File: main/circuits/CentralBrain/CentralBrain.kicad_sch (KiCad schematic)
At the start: 49 parts, among them J1 WAGO 12V IN, J2 WAGO 12V IN, J3 WAGE 12V IN, U1 MAX485E, U10 AM26C31CN, U11 AM26C31CN, U2 SN74HCT245N, U3 Teensy4.1_Minimal, U4 SN74HCT245N, U5 SN74HCT245N, U6 AM26C31CN, U7 AM26C31CN, U8 AM26C31CN, U9 AM26C31CN

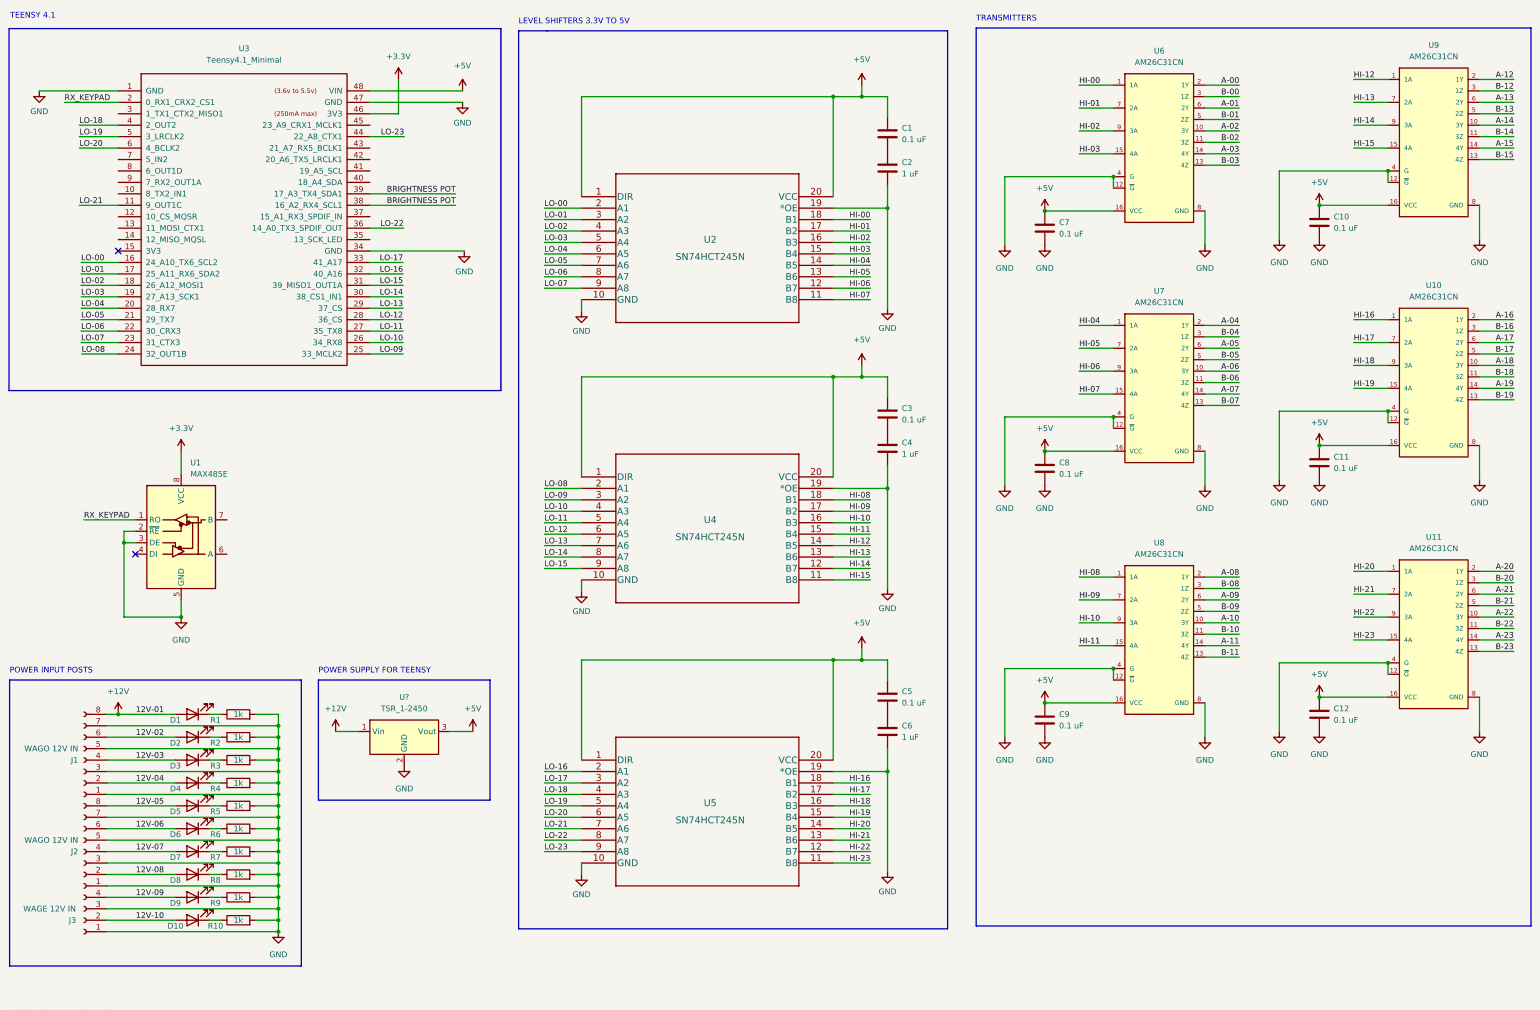
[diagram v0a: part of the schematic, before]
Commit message: no need for level shifters! thanks chuck!
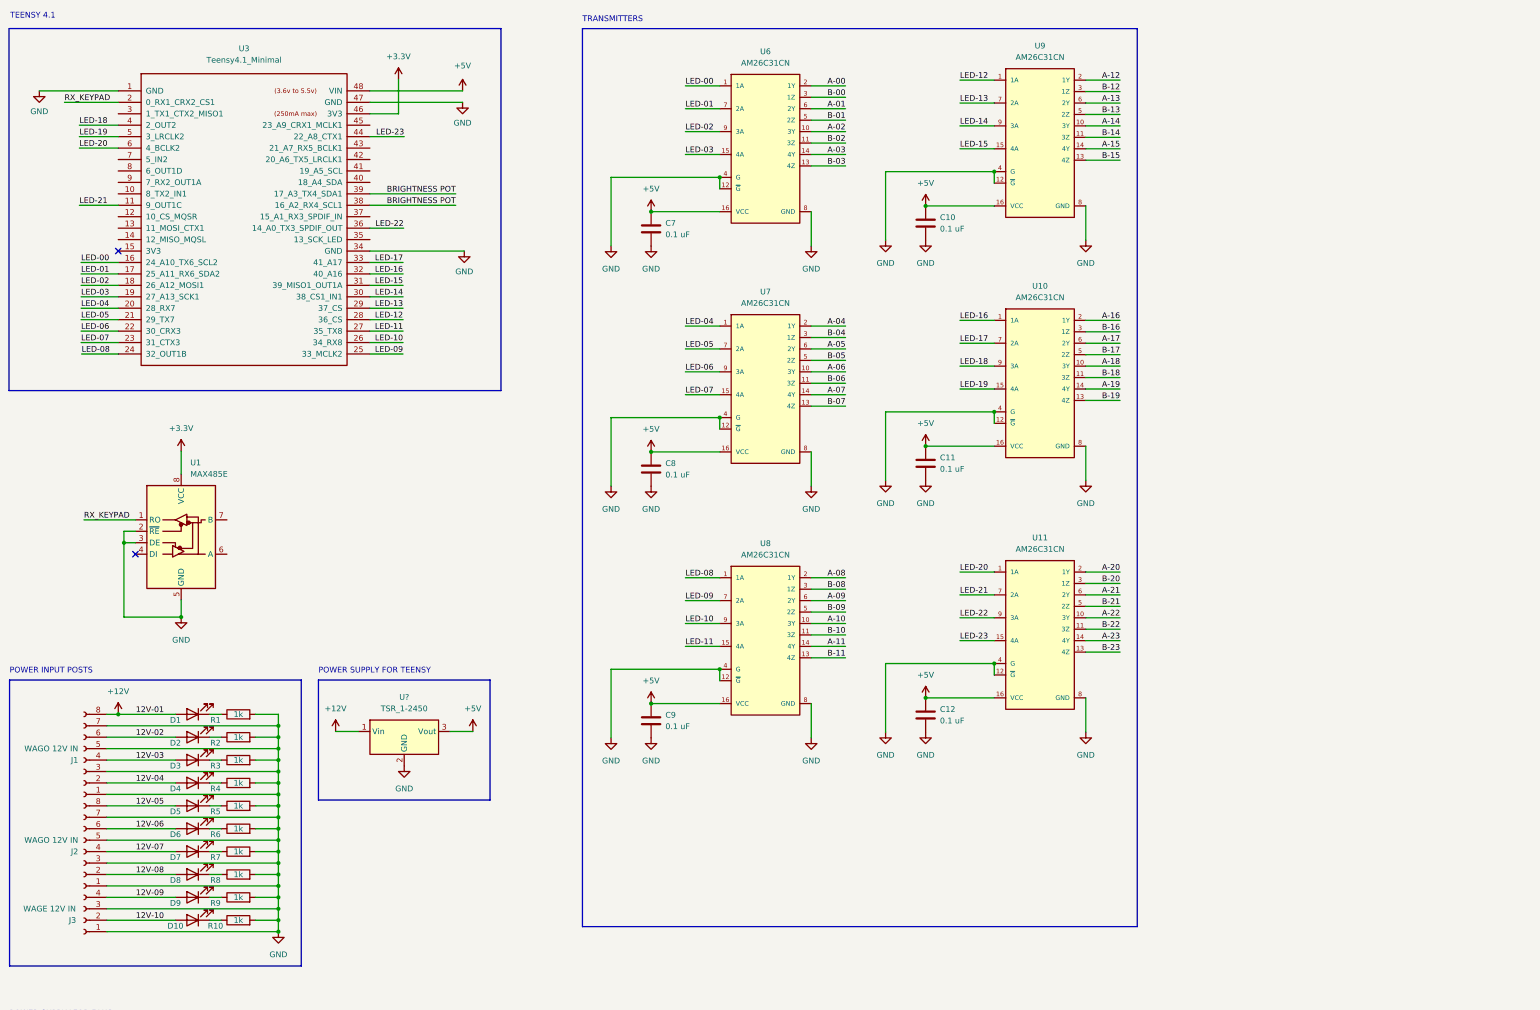
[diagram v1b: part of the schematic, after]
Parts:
- removed C1, C3, C5: 0.1 uF, symbol Device:C
- removed C2, C4, C6: 1 uF, symbol Device:C
- removed U2, U4, U5: SN74HCT245N, N20, symbol Joels KiCad Symbol Library:SN74HCT245N
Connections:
- net LO-00 is gone; now on net LED-00: U3.16 (24_A10_TX6_SCL2)
- net LO-01 is gone; now on net LED-01: U3.17 (25_A11_RX6_SDA2)
- net LO-02 is gone; now on net LED-02: U3.18 (26_A12_MOSI1)
- net LO-03 is gone; now on net LED-03: U3.19 (27_A13_SCK1)
- net LO-04 is gone; now on net LED-04: U3.20 (28_RX7)
- net LO-05 is gone; now on net LED-05: U3.21 (29_TX7)
- net LO-06 is gone; now on net LED-06: U3.22 (30_CRX3)
- net LO-07 is gone; now on net LED-07: U3.23 (31_CTX3)
- net LO-08 is gone; now on net LED-08: U3.24 (32_OUT1B)
- net LO-09 is gone; now on net LED-09: U3.25 (33_MCLK2)
- net LO-10 is gone; now on net LED-10: U3.26 (34_RX8)
- net LO-11 is gone; now on net LED-11: U3.27 (35_TX8)
- net LO-12 is gone; now on net LED-12: U3.28 (36_CS)
- net LO-13 is gone; now on net LED-13: U3.29 (37_CS)
- net LO-14 is gone; now on net LED-14: U3.30 (38_CS1_IN1)
- net LO-15 is gone; now on net LED-15: U3.31 (39_MISO1_OUT1A)
- net LO-16 is gone; now on net LED-16: U3.32 (40_A16)
- net LO-17 is gone; now on net LED-17: U3.33 (41_A17)
- net LO-18 is gone; now on net LED-18: U3.4 (2_OUT2)
- net LO-19 is gone; now on net LED-19: U3.5 (3_LRCLK2)
- net LO-20 is gone; now on net LED-20: U3.6 (4_BCLK2)
- net LO-21 is gone; now on net LED-21: U3.11 (9_OUT1C)
- net LO-22 is gone; now on net LED-22: U3.36 (14_A0_TX3_SPDIF_OUT)
- net LO-23 is gone; now on net LED-23: U3.44 (22_A8_CTX1)
- net HI-00 renamed LED-00
- net HI-01 renamed LED-01
- net HI-02 renamed LED-02
- net HI-03 renamed LED-03
- net HI-04 renamed LED-04
- net HI-05 renamed LED-05
- net HI-06 renamed LED-06
- net HI-07 renamed LED-07
- net HI-08 renamed LED-08
- net HI-09 renamed LED-09
- net HI-10 renamed LED-10
- net HI-11 renamed LED-11
- net HI-12 renamed LED-12
- net HI-13 renamed LED-13
- net HI-14 renamed LED-14
- net HI-15 renamed LED-15
- net HI-16 renamed LED-16
- net HI-17 renamed LED-17
- net HI-18 renamed LED-18
- net HI-19 renamed LED-19
- net HI-20 renamed LED-20
- net HI-21 renamed LED-21
- net HI-22 renamed LED-22
- net HI-23 renamed LED-23
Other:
- note removed: "LEVEL SHIFTERS 3.3V TO 5V"
- moved on the sheet: C10, C11, C12, C7, C8, C9, U10, U11, U6, U7, U8, U9

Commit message: started work on the central PCB
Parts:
- removed J1, J2: WAGO 12V IN, symbol Connector:Conn_01x08_Female
- removed J3: WAGE 12V IN, symbol Connector:Conn_01x04_Female
- removed J?: FAN, symbol Connector:Conn_01x02_Female
- removed U?: TSR_1-2450, Converter_DCDC:Converter_DCDC_TRACO_TSR-1_THT, symbol Regulator_Switching:TSR_1-2450
- added J1: POWER 1234, Joels KiCad Footprint Library:WAGO-2604-1308, symbol Joels KiCad Symbol Library:WAGO-2604-1308
- added J2: POWER 5678, Joels KiCad Footprint Library:WAGO-2604-1308, symbol Joels KiCad Symbol Library:WAGO-2604-1308
- added J3: POWER 910, Joels KiCad Footprint Library:WAGO-2604-1304, symbol Joels KiCad Symbol Library:WAGO-2604-1304
- added J4: EXTRA_TEENSY_PINS, Joels KiCad Footprint Library:CUI_term_block_8_TB004-508-08BE, symbol Connector:Conn_01x08_Female
- added J5: RJ45, Joels KiCad Footprint Library:TE_5569264-1_16_Port_RJ45, symbol Joels KiCad Symbol Library:TE_5569264-1_16_PORT_RJ45
- added J6: TE_5569262-1_08_PORT_RJ45, Joels KiCad Footprint Library:TE_5569262-1_08_Port_RJ45_New, symbol Joels KiCad Symbol Library:TE_5569262-1_08_PORT_RJ45
- added J7: RJ45_Shielded, Joels KiCad Footprint Library:RJ45-ASSMANN_A-2004-1-4-LP-N-R, symbol Connector:RJ45_Shielded
- added J8: AUDIO_PINS, Joels KiCad Footprint Library:CUI_term_block_8_TB004-508-08BE, symbol Connector:Conn_01x08_Female
- added RV1, RV2: 100K, Potentiometer_THT:Potentiometer_Alpha_RD901F-40-00D_Single_Vertical, symbol Device:R_Potentiometer_US
- added U5: Teensy4.0_AudioShield_REVD, Joels KiCad Footprint Library:Teensy4.0_Audioshield_RevD, symbol Joels KiCad Symbol Library:Teensy4.0_AudioShield_REVD
- C1: renamed from C7; footprint (none) -> Capacitor_SMD:C_0805_2012Metric_Pad1.18x1.45mm_HandSolder
- C2: renamed from C10; footprint (none) -> Capacitor_SMD:C_0805_2012Metric_Pad1.18x1.45mm_HandSolder
- C3: renamed from C8; footprint (none) -> Capacitor_SMD:C_0805_2012Metric_Pad1.18x1.45mm_HandSolder
- C4: renamed from C11; footprint (none) -> Capacitor_SMD:C_0805_2012Metric_Pad1.18x1.45mm_HandSolder
- C5: renamed from C9; footprint (none) -> Capacitor_SMD:C_0805_2012Metric_Pad1.18x1.45mm_HandSolder
- C6: renamed from C12; footprint (none) -> Capacitor_SMD:C_0805_2012Metric_Pad1.18x1.45mm_HandSolder
- D1, D10, D2, D3, D4, D5, D6, D7, D8, D9: footprint (none) -> LED_THT:LED_D3.0mm
- R1, R10, R2, R3, R4, R5, R6, R7, R8, R9: value 1k -> 4.7k; footprint (none) -> Resistor_THT:R_Axial_DIN0207_L6.3mm_D2.5mm_P7.62mm_Horizontal
- U1: footprint (none) -> Joels KiCad Footprint Library:Max485-Module
- U10, U11, U6, U7, U8, U9: footprint Texas_Instruments-AM26C31CDR-* -> Joels KiCad Footprint Library:AM26C31CN
- U3: footprint (none) -> Joels KiCad Footprint Library:Teensy41_Minimal
- gave numbers to parts that had none: 1
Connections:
- net +12V: now also J1.1, J1.2, J5.1, J5.10 (2), J5.11 (3), J5.2, J5.3, J5.9 (1), J7.1, J7.2, J7.3
- net +3V3: now also J8.1 (Pin_1), RV1.3, RV2.3, U5.28 (3V)
- net +5V: now also J4.1 (Pin_1)
- net 12V-02: now also J1.5, J1.6, J5.17 (1), J5.18 (2), J5.19 (3), J5.25 (1), J5.26 (2), J5.27 (3)
- net 12V-03: now also J1.10, J1.9, J5.33 (1), J5.34 (2), J5.35 (3), J5.41 (1), J5.42 (2), J5.43 (3)
- net 12V-04: now also J1.13, J1.14, J5.49 (1), J5.50 (2), J5.51 (3), J5.57 (1), J5.58 (2), J5.59 (3)
- net 12V-05: now also J2.1, J2.2, J5.65 (1), J5.66 (2), J5.67 (3), J5.73 (1), J5.74 (2), J5.75 (3)
- net 12V-06: now also J2.5, J2.6, J5.81 (1), J5.82 (2), J5.83 (3), J5.89 (1), J5.90 (2), J5.91 (3)
- net 12V-07: now also J2.10, J2.9, J5.105 (1), J5.106 (2), J5.107 (3), J5.113 (1), J5.114 (2), J5.115 (3), J5.97 (1), J5.98 (2), J5.99 (3)
- net 12V-08: now also J2.13, J2.14, J5.121 (1), J5.122 (2), J5.123 (3), J6.14, J6.15, J6.16, J6.6, J6.7, J6.8
- net 12V-09: now also J3.1, J3.2, J6.22, J6.23, J6.24, J6.30, J6.31, J6.32, J6.33, J6.34, J6.35
- net 12V-10: now also J3.5, J3.6, J6.41, J6.42, J6.43, J6.49, J6.50, J6.51, J6.57, J6.58, J6.59
- net A-00: now also J5.4
- net A-01: now also J5.12 (4)
- net A-02: now also J5.20 (4)
- net A-03: now also J5.28 (4)
- net A-04: now also J5.36 (4)
- net A-05: now also J5.44 (4)
- net A-06: now also J5.52 (4)
- net A-07: now also J5.60 (4)
- net A-08: now also J5.68 (4)
- net A-09: now also J5.76 (4)
- net A-10: now also J5.84 (4)
- net A-11: now also J5.92 (4)
- net A-12: now also J5.100 (4)
- net A-13: now also J5.108 (4)
- net A-14: now also J5.116 (4)
- net A-15: now also J5.124 (4)
- net A-16: now also J6.5
- net A-17: now also J6.36
- net A-18: now also J6.44
- net A-19: now also J6.13
- net A-20: now also J6.21
- net A-21: now also J6.52
- net A-22: now also J6.60
- net A-23: now also J6.29
- net B-00: now also J5.5
- net B-01: now also J5.13 (5)
- net B-02: now also J5.21 (5)
- net B-03: now also J5.29 (5)
- net B-04: now also J5.37 (5)
- net B-05: now also J5.45 (5)
- net B-06: now also J5.53 (5)
- net B-07: now also J5.61 (5)
- net B-08: now also J5.69 (5)
- net B-09: now also J5.77 (5)
- net B-10: now also J5.85 (5)
- net B-11: now also J5.93 (5)
- net B-12: now also J5.101 (5)
- net B-13: now also J5.109 (5)
- net B-14: now also J5.117 (5)
- net B-15: now also J5.125 (5)
- net B-16: now also J6.4
- net B-17: now also J6.37
- net B-18: now also J6.45
- net B-19: now also J6.12
- net B-20: now also J6.20
- net B-21: now also J6.53
- net B-22: now also J6.61
- net B-23: now also J6.28
- net GND: now also J1.11, J1.12, J1.15, J1.16, J1.3, J1.4, J1.7, J1.8, J2.11, J2.12, J2.15, J2.16, J2.3, J2.4, J2.7, J2.8, J3.3, J3.4, J3.7, J3.8, J4.8 (Pin_8), J5.102 (6), J5.103 (7), J5.104 (8), J5.110 (6), J5.111 (7), J5.112 (8), J5.118 (6), J5.119 (7), J5.120 (8), J5.126 (6), J5.127 (7), J5.128 (8), J5.14 (6), J5.15 (7), J5.16 (8), J5.22 (6), J5.23 (7), J5.24 (8), J5.30 (6), J5.31 (7), J5.32 (8), J5.38 (6), J5.39 (7), J5.40 (8), J5.46 (6), J5.47 (7), J5.48 (8), J5.54 (6), J5.55 (7), J5.56 (8), J5.6, J5.62 (6), J5.63 (7), J5.64 (8), J5.7, J5.70 (6), J5.71 (7), J5.72 (8), J5.78 (6), J5.79 (7), J5.8, J5.80 (8), J5.86 (6), J5.87 (7), J5.88 (8), J5.94 (6), J5.95 (7), J5.96 (8), J5.SH1 (SHIELD), J5.SH2 (SHIELD), J5.SH3 (SHIELD), J5.SH4 (SHIELD), J5.SH5 (SHIELD), J5.SH6 (SHIELD), J6.1, J6.10, J6.11, J6.17, J6.18, J6.19, J6.2, J6.25, J6.26, J6.27, J6.3, J6.38, J6.39, J6.40, J6.46, J6.47, J6.48, J6.54, J6.55, J6.56, J6.62, J6.63, J6.64, J6.67 (SH67), J6.68 (SH68), J6.69 (SH69), J6.70 (SH70), J6.71 (SH71), J6.72 (SH72), J6.9, J7.6, J7.7, J7.8, J7.S1, J7.S2, J8.6 (Pin_6), J8.7 (Pin_7), J8.8 (Pin_8), RV1.1, RV2.1, U5.1 (GND), U5.29 (GND)
- net at U1.6 (A): now also J7.5
- net at U1.7 (B): now also J7.4
- net AUDIO_DOUT: now reaches U3.10 (8_TX2_IN1)
- net AUDIO_DOUT: now also U5.10 (8_TX2_IN1)
- net PIN_10: now reaches U3.12 (10_CS_MQSR)
- net PIN_10: now also J4.2 (Pin_2)
- net PIN_11: now reaches U3.13 (11_MOSI_CTX1)
- net PIN_11: now also J4.3 (Pin_3)
- net PIN_12: now reaches U3.14 (12_MISO_MQSL)
- net PIN_12: now also J4.4 (Pin_4)
- net PIN_1: now reaches U3.3 (1_TX1_CTX2_MISO1)
- net PIN_1: now also J4.6 (Pin_6)
- net PIN_15: now reaches U3.37 (15_A1_RX3_SPDIF_IN)
- net PIN_15: now also J4.5 (Pin_5)
- net AUDIO_SDA: now reaches U3.40 (18_A4_SDA)
- net AUDIO_SDA: now also U5.22 (18_A4_SDA0)
- net AUDIO_SCL: now reaches U3.41 (19_A5_SCL)
- net AUDIO_SCL: now also U5.23 (19_A5_SCL0)
- net AUDIO_LRCLK: now reaches U3.42 (20_A6_TX5_LRCLK1)
- net AUDIO_LRCLK: now also U5.24 (20_A6_TX5_LRCLK1)
- net AUDIO_BCLK: now reaches U3.43 (21_A7_RX5_BCLK1)
- net AUDIO_BCLK: now also U5.25 (21_A7_RX5_BCLK1)
- net AUDIO_MCLK: now reaches U3.45 (23_A9_CRX1_MCLK1)
- net AUDIO_MCLK: now also U5.27 (23_A9_CRX1_MCLK1)
- net PHONE_JACK_SW: now reaches U3.7 (5_IN2)
- net PHONE_JACK_SW: now also J8.5 (Pin_5)
- net PIN_6: now reaches U3.8 (6_OUT1D)
- net PIN_6: now also J4.7 (Pin_7)
- net AUDIO_DIN: now reaches U3.9 (7_RX2_OUT1A)
- net AUDIO_DIN: now also U5.9 (7_RX2_OUT1A)
- net BRIGHTNESS POT renamed POT_ANTENNA
- net POT_ANTENNA: now also RV1.2; no longer U3.38 (16_A2_RX4_SCL1)
- new net AUDIO_LINE_IN_GND: J8.2 (Pin_2), U5.36 (LINE_IN_R_GND), U5.37 (LINE_IN_L_GND)
- new net AUDIO_LINE_IN_L: J8.3 (Pin_3), U5.35 (LINE_IN_L)
- new net AUDIO_LINE_IN_R: J8.4 (Pin_4), U5.34 (LINE_IN_R)
- new net POT_WHIPS: RV2.2, U3.38 (16_A2_RX4_SCL1)
- no-connect marks 2 -> 34
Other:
- note added: "A LOT OF RJ-45 OUTPUT"
- note added: "AUDIO PINS AND EXTRA PINS"
- note added: "AUDIO SHIELD"
- note added: "BRIGHTNESS POTENTIOMETERS"
- note added: "CONNECTION TO KEYBOARD"
- note added: "DC POWER SUPPLY CONNECTION"
- note added: "FOR ANTENNA"
- note added: "FOR WHIPS"
- note added: "POWER INDICATOR LAMPS"
- note added: "T568B COLOR CODE 1 ORA . . . 12V 2 ORA --- 12V 3 GRN . . . 12V 4 BLU --- A 5 BLU . . . B 6 GRN --- GND 7 BRN . . . GND 8 BRN --- GND"
- note removed: "POWER INPUT POSTS"
- note removed: "POWER SUPPLY FOR FANS"
- moved on the sheet: C1, C2, C3, C4, C5, C6, D1, D10, D2, D3, D4, D5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

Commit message: lots of work on pcb
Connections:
- net A-00: now also J5.20 (4); no longer J5.4
- net A-01: now also J5.84 (4); no longer J5.12 (4)
- net A-02: now also J5.92 (4); no longer J5.20 (4)
- net A-05: now also J5.100 (4); no longer J5.44 (4)
- net A-06: now also J5.108 (4); no longer J5.52 (4)
- net A-07: now also J5.44 (4); no longer J5.60 (4)
- net A-08: now also J5.4; no longer J5.68 (4)
- net A-09: now also J5.68 (4); no longer J5.76 (4)
- net A-10: now also J5.76 (4); no longer J5.84 (4)
- net A-11: now also J5.12 (4); no longer J5.92 (4)
- net A-12: now also J5.52 (4); no longer J5.100 (4)
- net A-13: now also J5.116 (4); no longer J5.108 (4)
- net A-14: now also J5.124 (4); no longer J5.116 (4)
- net A-15: now also J5.60 (4); no longer J5.124 (4)
- net B-00: now also J5.21 (5); no longer J5.5
- net B-01: now also J5.85 (5); no longer J5.13 (5)
- net B-02: now also J5.93 (5); no longer J5.21 (5)
- net B-05: now also J5.101 (5); no longer J5.45 (5)
- net B-06: now also J5.109 (5); no longer J5.53 (5)
- net B-07: now also J5.45 (5); no longer J5.61 (5)
- net B-08: now also J5.5; no longer J5.69 (5)
- net B-09: now also J5.69 (5); no longer J5.77 (5)
- net B-10: now also J5.77 (5); no longer J5.85 (5)
- net B-11: now also J5.13 (5); no longer J5.93 (5)
- net B-12: now also J5.53 (5); no longer J5.101 (5)
- net B-13: now also J5.117 (5); no longer J5.109 (5)
- net B-14: now also J5.125 (5); no longer J5.117 (5)
- net B-15: now also J5.61 (5); no longer J5.125 (5)
- net LED-00: now also U3.30 (38_CS1_IN1); no longer U3.16 (24_A10_TX6_SCL2)
- net LED-01: now also U3.31 (39_MISO1_OUT1A); no longer U3.17 (25_A11_RX6_SDA2)
- net LED-02: now also U3.28 (36_CS); no longer U3.18 (26_A12_MOSI1)
- net LED-03: now also U3.29 (37_CS); no longer U3.19 (27_A13_SCK1)
- net LED-04: now also U3.26 (34_RX8); no longer U3.20 (28_RX7)
- net LED-05: now also U3.27 (35_TX8); no longer U3.21 (29_TX7)
- net LED-06: now also U3.24 (32_OUT1B); no longer U3.22 (30_CRX3)
- net LED-07: now also U3.25 (33_MCLK2); no longer U3.23 (31_CTX3)
- net LED-08: now also U3.36 (14_A0_TX3_SPDIF_OUT); no longer U3.24 (32_OUT1B)
- net LED-09: now also U3.44 (22_A8_CTX1); no longer U3.25 (33_MCLK2)
- net LED-10: now also U3.32 (40_A16); no longer U3.26 (34_RX8)
- net LED-11: now also U3.33 (41_A17); no longer U3.27 (35_TX8)
- net LED-12: now also U3.22 (30_CRX3); no longer U3.28 (36_CS)
- net LED-13: now also U3.23 (31_CTX3); no longer U3.29 (37_CS)
- net LED-14: now also U3.20 (28_RX7); no longer U3.30 (38_CS1_IN1)
- net LED-15: now also U3.21 (29_TX7); no longer U3.31 (39_MISO1_OUT1A)
- net LED-16: now also U3.18 (26_A12_MOSI1); no longer U3.32 (40_A16)
- net LED-17: now also U3.19 (27_A13_SCK1); no longer U3.33 (41_A17)
- net LED-18: now also U3.16 (24_A10_TX6_SCL2); no longer U3.4 (2_OUT2)
- net LED-19: now also U3.17 (25_A11_RX6_SDA2); no longer U3.5 (3_LRCLK2)
- net LED-22: now also U3.4 (2_OUT2); no longer U3.36 (14_A0_TX3_SPDIF_OUT)
- net LED-23: now also U3.5 (3_LRCLK2); no longer U3.44 (22_A8_CTX1)

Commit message: Mechanical design of PCB mostly done
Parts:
- added H1, H3, H4, H6: MountingHole, MountingHole:MountingHole_3.5mm, symbol Mechanical:MountingHole
- J6: footprint Joels KiCad Footprint Library:TE_5569262-1_08_Port_RJ45_New -> Joels KiCad Footprint Library:TE_5569262-1_08_Port_RJ45
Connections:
- net +12V: now also J5.121 (1), J5.122 (2), J5.123 (3), J5.49 (1), J5.50 (2), J5.51 (3), J5.57 (1), J5.58 (2), J5.59 (3); no longer J5.1, J5.10 (2), J5.11 (3), J5.2, J5.3, J5.9 (1)
- net LED-00: now also U3.24 (32_OUT1B); no longer U3.30 (38_CS1_IN1)
- net LED-01: now also U3.25 (33_MCLK2); no longer U3.31 (39_MISO1_OUT1A)
- net LED-02: now also U3.26 (34_RX8); no longer U3.28 (36_CS)
- net LED-03: now also U3.27 (35_TX8); no longer U3.29 (37_CS)
- net LED-04: now also U3.28 (36_CS); no longer U3.26 (34_RX8)
- net LED-05: now also U3.29 (37_CS); no longer U3.27 (35_TX8)
- net LED-06: now also U3.30 (38_CS1_IN1); no longer U3.24 (32_OUT1B)
- net LED-07: now also U3.31 (39_MISO1_OUT1A); no longer U3.25 (33_MCLK2)
- net LED-08: now also U3.20 (28_RX7); no longer U3.36 (14_A0_TX3_SPDIF_OUT)
- net LED-09: now also U3.21 (29_TX7); no longer U3.44 (22_A8_CTX1)
- net LED-10: now also U3.22 (30_CRX3); no longer U3.32 (40_A16)
- net LED-11: now also U3.23 (31_CTX3); no longer U3.33 (41_A17)
- net LED-12: now also U3.32 (40_A16); no longer U3.22 (30_CRX3)
- net LED-13: now also U3.33 (41_A17); no longer U3.23 (31_CTX3)
- net LED-14: now also U3.36 (14_A0_TX3_SPDIF_OUT); no longer U3.20 (28_RX7)
- net LED-15: now also U3.44 (22_A8_CTX1); no longer U3.21 (29_TX7)
- net LED-16: now also U3.4 (2_OUT2); no longer U3.18 (26_A12_MOSI1)
- net LED-17: now also U3.5 (3_LRCLK2); no longer U3.19 (27_A13_SCK1)
- net LED-18: now also U3.6 (4_BCLK2); no longer U3.16 (24_A10_TX6_SCL2)
- net LED-19: now also U3.11 (9_OUT1C); no longer U3.17 (25_A11_RX6_SDA2)
- net LED-20: now also U3.16 (24_A10_TX6_SCL2); no longer U3.6 (4_BCLK2)
- net LED-21: now also U3.17 (25_A11_RX6_SDA2); no longer U3.11 (9_OUT1C)
- net LED-22: now also U3.18 (26_A12_MOSI1); no longer U3.4 (2_OUT2)
- net LED-23: now also U3.19 (27_A13_SCK1); no longer U3.5 (3_LRCLK2)
- net PIN_1: now also J4.2 (Pin_2); no longer J4.6 (Pin_6)
- net PIN_10: now also J4.4 (Pin_4); no longer J4.2 (Pin_2)
- net PIN_11: now also J4.5 (Pin_5); no longer J4.3 (Pin_3)
- net PIN_12: now also J4.6 (Pin_6); no longer J4.4 (Pin_4)
- net PIN_15: now also J4.7 (Pin_7); no longer J4.5 (Pin_5)
- net PIN_6: now also J4.3 (Pin_3); no longer J4.7 (Pin_7)
- removed net 12V-02: D2.2 (A), J1.5, J1.6, J5.17 (1), J5.18 (2), J5.19 (3), J5.25 (1), J5.26 (2), J5.27 (3)
- net 12V-03 renamed 12V_03
- net 12V_03: now also J5.25 (1), J5.26 (2), J5.27 (3), J5.97 (1), J5.98 (2), J5.99 (3); no longer J5.41 (1), J5.42 (2), J5.43 (3)
- removed net 12V-04: D4.2 (A), J1.13, J1.14, J5.49 (1), J5.50 (2), J5.51 (3), J5.57 (1), J5.58 (2), J5.59 (3)
- net 12V-05 renamed 12V_05
- net 12V_05: now also J5.10 (2), J5.11 (3), J5.9 (1); no longer J5.65 (1), J5.66 (2), J5.67 (3)
- net 12V-06 renamed 12V_04
- net 12V_04: now also D4.2 (A), J1.13, J1.14, J5.17 (1), J5.18 (2), J5.19 (3); no longer D6.2 (A), J2.5, J2.6
- net 12V-07 renamed 12V_02
- net 12V_02: now also D2.2 (A), J1.5, J1.6, J5.41 (1), J5.42 (2), J5.43 (3); no longer D7.2 (A), J2.10, J2.9, J5.97 (1), J5.98 (2), J5.99 (3)
- removed net 12V-08: D8.2 (A), J2.13, J2.14, J5.121 (1), J5.122 (2), J5.123 (3), J6.14, J6.15, J6.16, J6.6, J6.7, J6.8
- removed net 12V-09: D9.2 (A), J3.1, J3.2, J6.22, J6.23, J6.24, J6.30, J6.31, J6.32, J6.33, J6.34, J6.35
- removed net 12V-10: D10.2 (A), J3.5, J3.6, J6.41, J6.42, J6.43, J6.49, J6.50, J6.51, J6.57, J6.58, J6.59
- new net 12V_06: D6.2 (A), J2.5, J2.6, J5.1, J5.2, J5.3, J5.65 (1), J5.66 (2), J5.67 (3)
- new net 12V_07: D7.2 (A), J2.10, J2.9, J6.30, J6.31, J6.32, J6.57, J6.58, J6.59
- new net 12V_08: D8.2 (A), J2.13, J2.14, J6.22, J6.23, J6.24, J6.49, J6.50, J6.51
- new net 12V_09: D9.2 (A), J3.1, J3.2, J6.14, J6.15, J6.16, J6.41, J6.42, J6.43
- new net 12V_10: D10.2 (A), J3.5, J3.6, J6.33, J6.34, J6.35, J6.6, J6.7, J6.8
- no-connect marks 34 -> 32
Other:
- note added: "MOUNTING HOLES"
- note removed: "FOR ANTENNA"
- note removed: "FOR WHIPS"
